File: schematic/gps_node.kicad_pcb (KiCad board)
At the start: 2 copper layers, 48 x 75 mm, 84 parts, among them IC1 MMA8452Q, IC2 MCP73831/2, J1 USB_OTG, J10 Mounting Hole, J11 TEST Vbatt, J12 Test 3.3v, J13 Test Gnd, J14 UART RF, J15 I2C GPS, J16 UART GPS, J17 GPIO_0, J18 GPIO_1, J2 AVR ICSP, J3 LIPO_BAT, J4 SOLAR, J5 FW_UPDATE, J6 SMA, J7 Mounting Hole, J8 Mounting Hole, J9 Mounting Hole, SW1 SW_SP3T, SW2 RESET, SW3 RESET, SW4 RESET, U1 TLV71333PDBV, U2 ublox-cam-m8q-0, U3 ATMEGA32U4-AU, U4 RN2483, Y1 16MHz

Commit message: Start initial pcb layout
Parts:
- removed the C18 at (120.4, 98.8)
- removed the D1 at (109.0, 87.4)
- removed the D2 at (108.7, 93.7)
- removed the D3 at (113.0, 90.2)
- removed the IC1 at (124.7, 99.3)
- removed the J15 at (144.8, 119.4)
- removed J18: GPIO_1, Pin_Headers:Pin_Header_Straight_1x02_Pitch2.54mm
- removed the J6 at (133.3, 66.0)
- removed LED1: WS2812B, LEDs:LED_WS2812B-PLCC4
- removed the R10 at (121.9, 80.0)
- removed the R12 at (121.9, 82.3)
- removed the R18 at (131.3, 71.9)
- removed R19: 0, Resistors_SMD:R_0805
- removed R22, R23: 4.7k, Resistors_SMD:R_0805
- removed the R8 at (129.5, 97.5)
- removed the R9 at (129.5, 100.3)
- removed the SW3 at (123.8, 130.8)
- added C1: NFM21HC105R1C3D, gps_node_components:C_FEEDTHROUGH_0805, F.Cu at (130.3, 77.5)
- added C19: NFM21HC105R1C3D, gps_node_components:C_FEEDTHROUGH_0805, B.Cu at (136.4, 118.1)
- added C21: 100nF, Capacitors_SMD:C_0805, F.Cu at (135.4, 73.7)
- added D4: LED_Small_ALT, LEDs:LED_0805, B.Cu at (90.2, 87.6)
- added J10: Test V_RN, Socket_Strips:Socket_Strip_Straight_1x01_Pitch2.54mm, F.Cu at (181.7, 114.8)
- added J9: Test V_bak, Socket_Strips:Socket_Strip_Straight_1x01_Pitch2.54mm, F.Cu at (186.8, 122.4)
- added U3: TLV71333PDBV, TO_SOT_Packages_SMD:SOT-23-5, F.Cu at (135.4, 77.0)
- C12, C5: moved to B.Cu
- C3, F1: moved to F.Cu
- J17: value GPIO_0 -> Conn_Coaxial; footprint Pin_Headers:Pin_Header_Straight_1x02_Pitch2.54mm -> gps_node_components:CONN-RF-UFL
- R1: value 4.7k -> 10k; moved to F.Cu
- R11: renamed from R26; value 4.7k -> 10k
- R13: renamed from R2; value 4.7k -> 470
- R6: renamed from R7; value 4.7k -> 10k
- SW1: value SW_SP3T -> SW_SPDT; footprint gps_node_components:DP3T_switch -> Pin_Headers:Pin_Header_Straight_1x03_Pitch2.54mm
- moved C14 56.0 mm to (74.0, 106.7)
- moved C15 56.0 mm to (67.7, 106.7)
- moved C7 56.0 mm to (64.1, 103.7)
- moved R12 56.0 mm to (69.0, 95.8)
- moved R18 56.0 mm to (65.7, 97.6)
- moved Y1 56.0 mm to (70.4, 106.7)
- moved C10 56.0 mm to (76.5, 86.4)
- moved J16 52.0 mm to (102.1, 111.0)
- moved J15 49.6 mm to (110.7, 73.2)
- moved R10 47.4 mm to (105.2, 112.0)
- moved U4 45.7 mm to (170.2, 113.0)
- moved J5 42.2 mm to (152.4, 128.3)
- moved C6 42.1 mm to (180.9, 88.1)
- moved C8 42.1 mm to (183.7, 88.1)
- moved J11 42.1 mm to (181.7, 127.5)
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- renumbered C19 to C18, C1 to C2, C2 to C4, D4 to D1, D5 to D2, D6 to D3, D7 to D5, D8 to D6, IC2 to IC1, J7 to J1, J2 to J11, J14 to J12, J3 to J13, J4 to J14, J16 to J15, J5 to J16, J8 to J2, J9 to J3, J10 to J4, J11 to J5, J1 to J6, J12 to J7, J13 to J8, R25 to R10, R14 to R12, R15 to R14, R16 to R15, R17 to R16, R20 to R17, R21 to R18, R3 to R2, R4 to R3, R5 to R4, R6 to R5, R11 to R7, R24 to R8, R13 to R9, SW4 to SW3, U3 to U4, U4 to U5
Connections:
- C12 pad 1: +3V3 -> /V_RN
- C13 pad 1: +3V3 -> Net-(C1-Pad3)
- C3 pad 1: +3V3 -> Net-(C1-Pad3)
- C5 pad 1: +3V3 -> /V_RN
- J1 pad 1: Net-(J7-Pad1) -> (no net)
- J16 pad 2: +3V3 -> /V_RN
- J16 pad 6: Net-(J5-Pad6) -> (no net)
- J17 pad 1: /IN_0 -> Net-(J17-Pad1)
- J2 pad 1: Net-(J8-Pad1) -> (no net)
- J3 pad 1: Net-(J9-Pad1) -> (no net)
- J4 pad 1: Net-(J10-Pad1) -> (no net)
- J6 pad 4: Net-(J1-Pad4) -> (no net)
- R1 pad 1: /MCU_PWSEL0_IN -> /REG_ENABLE
- R1 pad 2: Net-(D1-Pad2) -> GND
- R10 pad 2: +3V3 -> /V_RN
- R12 pad 2: /LED_OUT -> /LED_OUT_RED
- R13 pad 1: /MCU_PWSEL11_IN -> Net-(D4-Pad1)
- R13 pad 2: Net-(D2-Pad2) -> /LED_OUT_GRN
- SW1 pad 1: Net-(SW1-Pad1) -> (no net)
- SW1 pad 2: Net-(D1-Pad2) -> +BATT
- SW1 pad 3: +BATT -> /REG_ENABLE
- U1 pad 4: Net-(U1-Pad4) -> (no net)
- U2 pad 1: +3V3 -> Net-(C1-Pad3)
- U2 pad 2: Net-(U2-Pad2) -> (no net)
- U2 pad 20: Net-(U2-Pad20) -> (no net)
- U2 pad 23: Net-(U2-Pad23) -> (no net)
- U2 pad 24: Net-(U2-Pad24) -> (no net)
- U2 pad 28: Net-(U2-Pad28) -> (no net)
- U2 pad 29: Net-(U2-Pad29) -> (no net)
- U2 pad 3: /I2C_GPS_SDA -> (no net)
- U2 pad 30: Net-(U2-Pad30) -> (no net)
- U2 pad 6: /I2C_GPS_SCL -> (no net)
- U2 pad 7: Net-(U2-Pad7) -> (no net)
- U2 pad 8: +3V3 -> /V_bak
- U2 pad 9: +3V3 -> Net-(C1-Pad3)
- U4 pad 1: /RGB_LED -> (no net)
- U4 pad 12: /ACC_INT2 -> (no net)
- U4 pad 18: /I2C_GPS_SCL -> /BUTTON_1
- U4 pad 19: /I2C_GPS_SDA -> (no net)
- U4 pad 22: /LED_OUT -> (no net)
- U4 pad 25: /MCU__OUT -> (no net)
- U4 pad 26: /MCU_PWSEL11_IN -> (no net)
- U4 pad 27: /MCU_PWSEL0_IN -> (no net)
- U4 pad 28: /ACC_INT1 -> (no net)
- U4 pad 32: Net-(U3-Pad32) -> (no net)
- U4 pad 33: Net-(U3-Pad33) -> (no net)
- U4 pad 36: /IN_1 -> /LED_OUT_GRN
- U4 pad 37: /IN_0 -> /LED_OUT_RED
- U4 pad 38: Net-(U3-Pad38) -> (no net)
- U4 pad 39: /BUTTON_1 -> (no net)
- U4 pad 8: Net-(U3-Pad8) -> (no net)
- U5 pad 10: Net-(U4-Pad10) -> (no net)
- U5 pad 12: +3V3 -> /V_RN
- U5 pad 13: Net-(U4-Pad13) -> (no net)
- U5 pad 14: Net-(U4-Pad14) -> (no net)
- U5 pad 15: Net-(U4-Pad15) -> (no net)
- U5 pad 16: Net-(U4-Pad16) -> (no net)
- U5 pad 17: Net-(U4-Pad17) -> (no net)
- U5 pad 18: Net-(U4-Pad18) -> (no net)
- U5 pad 19: Net-(U4-Pad19) -> (no net)
- U5 pad 2: Net-(U4-Pad2) -> (no net)
- U5 pad 23: Net-(R19-Pad1) -> Net-(J17-Pad1)
- U5 pad 25: Net-(R18-Pad1) -> (no net)
- U5 pad 29: Net-(U4-Pad29) -> (no net)
- U5 pad 3: Net-(U4-Pad3) -> (no net)
- U5 pad 34: +3V3 -> /V_RN
- U5 pad 35: Net-(U4-Pad35) -> (no net)
- U5 pad 36: Net-(U4-Pad36) -> (no net)
- U5 pad 37: Net-(U4-Pad37) -> (no net)
- U5 pad 38: Net-(U4-Pad38) -> (no net)
- U5 pad 39: Net-(U4-Pad39) -> (no net)
- U5 pad 4: Net-(U4-Pad4) -> (no net)
- U5 pad 40: Net-(U4-Pad40) -> (no net)
- U5 pad 42: Net-(U4-Pad42) -> (no net)
- U5 pad 43: Net-(U4-Pad43) -> (no net)
- U5 pad 44: Net-(U4-Pad44) -> (no net)
- U5 pad 45: Net-(U4-Pad45) -> (no net)
- U5 pad 46: Net-(U4-Pad46) -> (no net)
- U5 pad 5: Net-(U4-Pad5) -> (no net)
- U5 pad 9: Net-(U4-Pad9) -> (no net)
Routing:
- net GND: track 532.2 -> 0.00 mm, vias 66 -> 0
- net +3V3: track 197.3 -> 0.00 mm, vias 10 -> 0
- net /I2C_GPS_SCL: track 115.0 -> 0.00 mm, vias 2 -> 0
- net /I2C_GPS_SDA: track 106.0 -> 0.00 mm, vias 2 -> 0
- net +BATT: track 65.8 -> 0.00 mm, vias 3 -> 0
- net /UART_AT_TO_RN: track 76.1 -> 13.4 mm, vias 3 -> 0
- net /UART_RN_TO_AT: track 71.2 -> 13.7 mm, vias 3 -> 0
- net /UART_GPS_OUT: track 65.8 -> 8.58 mm, vias 2 -> 0
- net /UART_GPS_IN: track 61.6 -> 10.2 mm
- net /MCU_PWSEL11_IN: track 48.4 -> 0.00 mm, vias 3 -> 0
- net /RESET: track 46.5 -> 0.00 mm, vias 3 -> 0
- net /MCU_PWSEL0_IN: track 46.2 -> 0.00 mm, vias 3 -> 0
- net /V_RN: track 0.00 -> 44.2 mm
- net /charge_status: track 42.8 -> 0.00 mm, vias 4 -> 0
- net /MCU__OUT: track 42.5 -> 0.00 mm, vias 2 -> 0
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- removed copper zone on B.Cu, net GND
- removed copper zone on F.Cu, net GND

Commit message: PCB layout finsihed
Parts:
- removed J10: Test V_RN, Socket_Strips:Socket_Strip_Straight_1x01_Pitch2.54mm
- removed R7, R9: 0, Resistors_SMD:R_0805
- removed R8: 470, Resistors_SMD:R_0805
- C10, C20, D3, D4, D5, D6, R11, R12, R13, R15, R16, R18: moved to F.Cu
- C18: value 4.7uF -> 10uF
- D1: value D_Small -> BAS K73; footprint gps_node_components:DB2J411 -> Diodes_SMD:D_SOT-23_ANK
- D2: value D_Small -> BAS K73; footprint gps_node_components:DB2J411 -> Diodes_SMD:D_SOT-23_ANK; moved to F.Cu
- J13, J14: footprint Pin_Headers:Pin_Header_Straight_1x02_Pitch2.54mm -> Connectors_Molex:Molex_PicoBlade_53047-0210_02x1.25mm_Straight
- SW3: value RESET -> MODE; moved to F.Cu
- moved J9 73.2 mm to (131.7, 74.2)
- moved C6 67.5 mm to (113.5, 91.7), turned to 90 degrees
- moved C7 64.2 mm to (123.6, 79.4), turned to 180 degrees
- moved J5 62.3 mm to (106.0, 86.6)
- moved C10 59.4 mm to (135.9, 85.1)
- moved C14 59.1 mm to (133.1, 105.7), turned to 0 degrees
- moved Y1 58.9 mm to (129.3, 104.4)
- moved C11 58.7 mm to (140.0, 97.0), turned to 0 degrees
- moved J11 58.5 mm to (142.5, 84.1), turned to 0 degrees
- moved C15 57.8 mm to (125.5, 105.7), turned to 180 degrees
- moved C8 57.2 mm to (126.6, 85.1), turned to 90 degrees
- moved R16 56.8 mm to (120.1, 80.5), turned to 0 degrees
- moved C20 52.1 mm to (119.8, 82.4), turned to 0 degrees
- moved R12 51.2 mm to (113.0, 121.9), turned to 270 degrees
- moved R6 50.6 mm to (127.8, 112.3), turned to 270 degrees
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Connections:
- D3 pad 1: Net-(D3-Pad1) -> GND
- D3 pad 2: +3V3 -> Net-(D3-Pad2)
- D4 pad 1: Net-(D4-Pad1) -> GND
- D4 pad 2: +3V3 -> Net-(D4-Pad2)
- J13 pad 1: Net-(J13-Pad1) -> +BATT
- J14 pad 1: Net-(J14-Pad1) -> /V_Solar
- R12 pad 1: Net-(D3-Pad1) -> Net-(D3-Pad2)
- R13 pad 1: Net-(D4-Pad1) -> Net-(D4-Pad2)
- U2 pad 4: Net-(U2-Pad4) -> GND
- U2 pad 5: Net-(U2-Pad4) -> GND
- U4 pad 31: Net-(R8-Pad2) -> /RN_RESET
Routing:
- net GND: track 0.00 -> 449.3 mm, vias 0 -> 200
- net +3V3: track 0.00 -> 140.0 mm, vias 0 -> 5
- net +BATT: track 0.00 -> 94.7 mm, vias 0 -> 2
- net /RN_RESET: track 23.7 -> 88.3 mm, vias 0 -> 5
- net /LED_OUT_GRN: track 0.00 -> 59.7 mm, vias 0 -> 2
- net /LED_OUT_RED: track 0.00 -> 56.4 mm, vias 0 -> 2
- net VBUS: track 0.00 -> 55.0 mm, vias 0 -> 3
- net /RESET: track 0.00 -> 54.7 mm, vias 0 -> 4
- net /charge_status: track 0.00 -> 52.9 mm, vias 0 -> 2
- net /UART_GPS_OUT: track 8.58 -> 49.0 mm
- net /UART_GPS_IN: track 10.2 -> 46.2 mm
- net /BUTTON_1: track 0.00 -> 35.3 mm, vias 0 -> 2
- net /MOSI: track 0.00 -> 33.1 mm, vias 0 -> 1
- net /MISO: track 0.00 -> 29.3 mm, vias 0 -> 2
- net /V_Solar: track 0.00 -> 29.2 mm, vias 0 -> 2
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- added copper zone on B.Cu, net GND
- added copper zone on F.Cu, net GND

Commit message: Clean up silkscreen
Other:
- board text added: "868MHz Antenna"
- board text added: "Batt"
- board text added: "IN"
- board text added: "ON"
- board text added: "OUT"
- board text added: "Off"
- board text added: "Solar"
- board text added: "TTN Tracker Node v1.2 http://ttntracker.com"
- board text added: "⇈ GPS Keep upright"
- board text removed: "In_0"
- board text removed: "In_1"
- board text removed: "RX"
- board text removed: "SCL"
- board text removed: "SDA"
- board text removed: "TTN Tracker Node v1 http://ttntracker.com"
- board text removed: "TX"

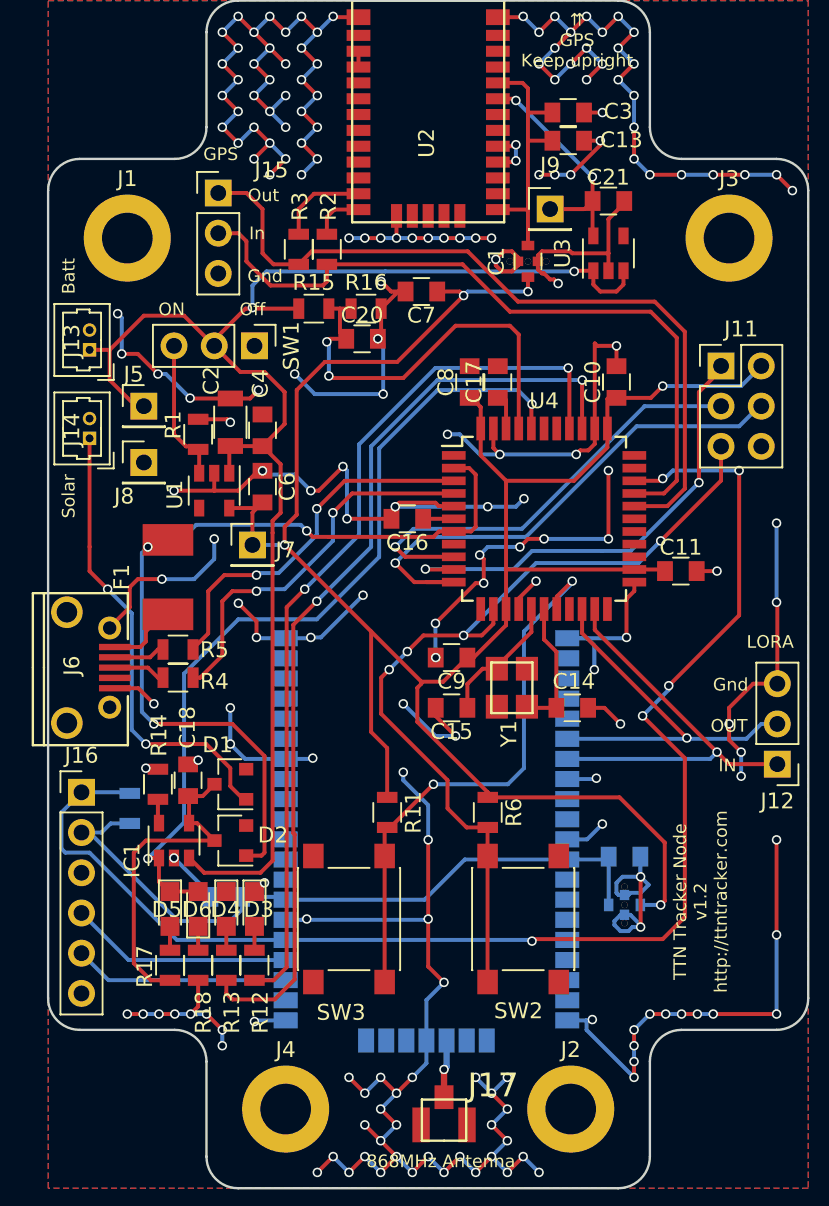
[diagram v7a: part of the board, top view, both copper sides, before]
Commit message: Further silkscreen cleanup
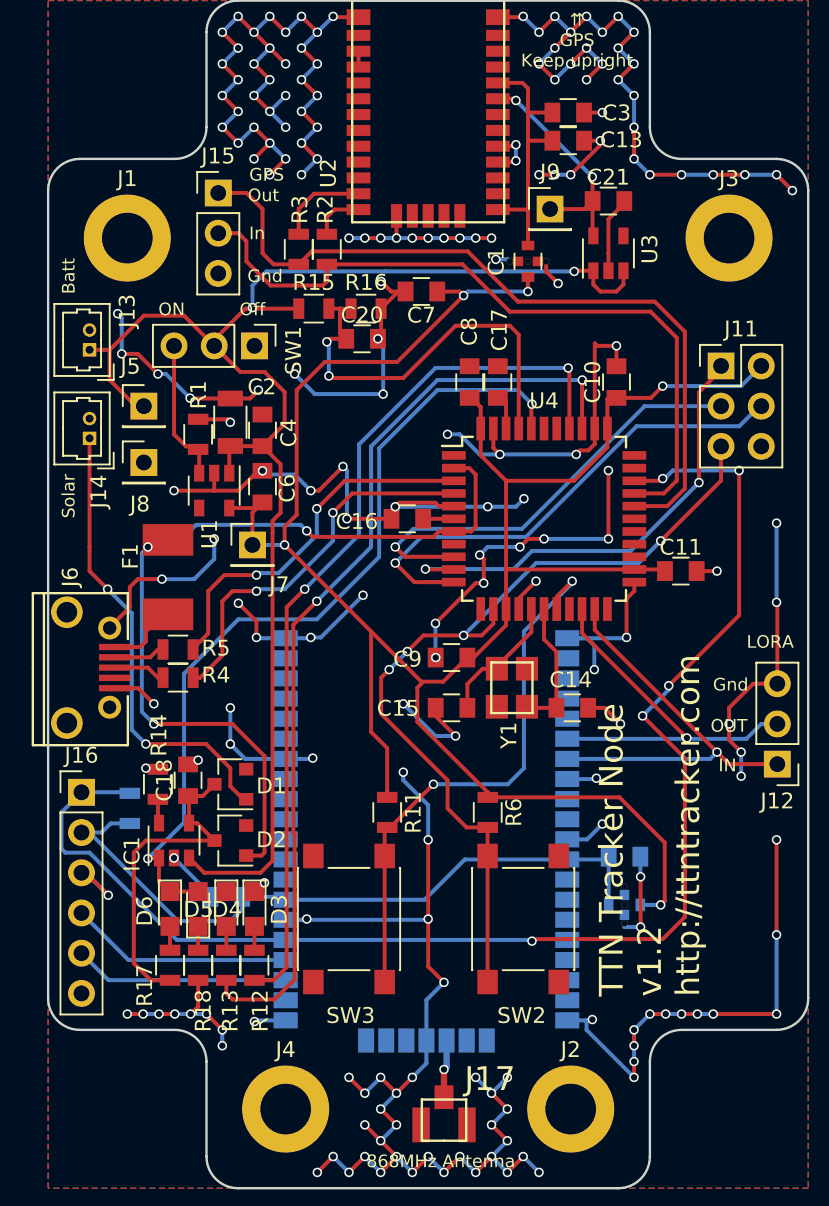
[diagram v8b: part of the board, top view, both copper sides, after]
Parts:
- J17: value Conn_Coaxial -> u.FL connector
- SW1: value SW_SPDT -> RS stock no. 448-0747
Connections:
- J1 pad 1: (no net) -> GND
- J2 pad 1: (no net) -> GND
- J3 pad 1: (no net) -> GND
- J4 pad 1: (no net) -> GND
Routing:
- net GND: track 449.3 -> 437.6 mm, vias 200 -> 201
